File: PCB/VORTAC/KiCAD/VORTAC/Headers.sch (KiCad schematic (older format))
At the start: 27 parts, among them J1 DEBUG, J10 FAN_01_V, J11 FAN_02_V, J12 LED_V, J13 THERM_R, J14 918-418K2023S40001, J15 STEPPER, J16 IO, J2 Molex Micro Fit 3.0, J3 MillMax_004, J4 MillMax_004, J5 USB_HOST, J6 HOTEND, J7 FAN_01, J8 FAN_02, J9 LED

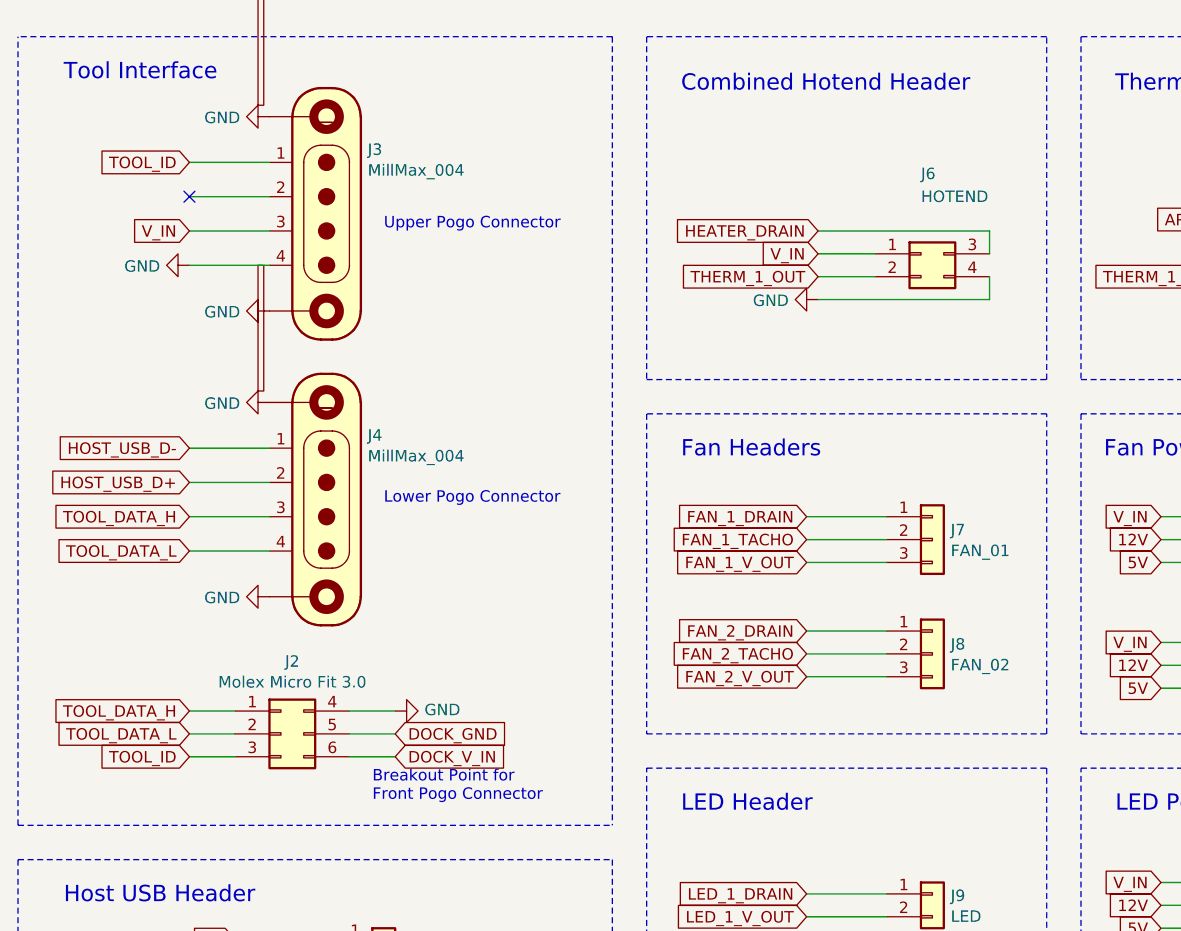
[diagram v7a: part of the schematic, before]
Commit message: Layouting & Footprints
-Improved Thermal Footprint Conductivity
-Improved Component Spacing
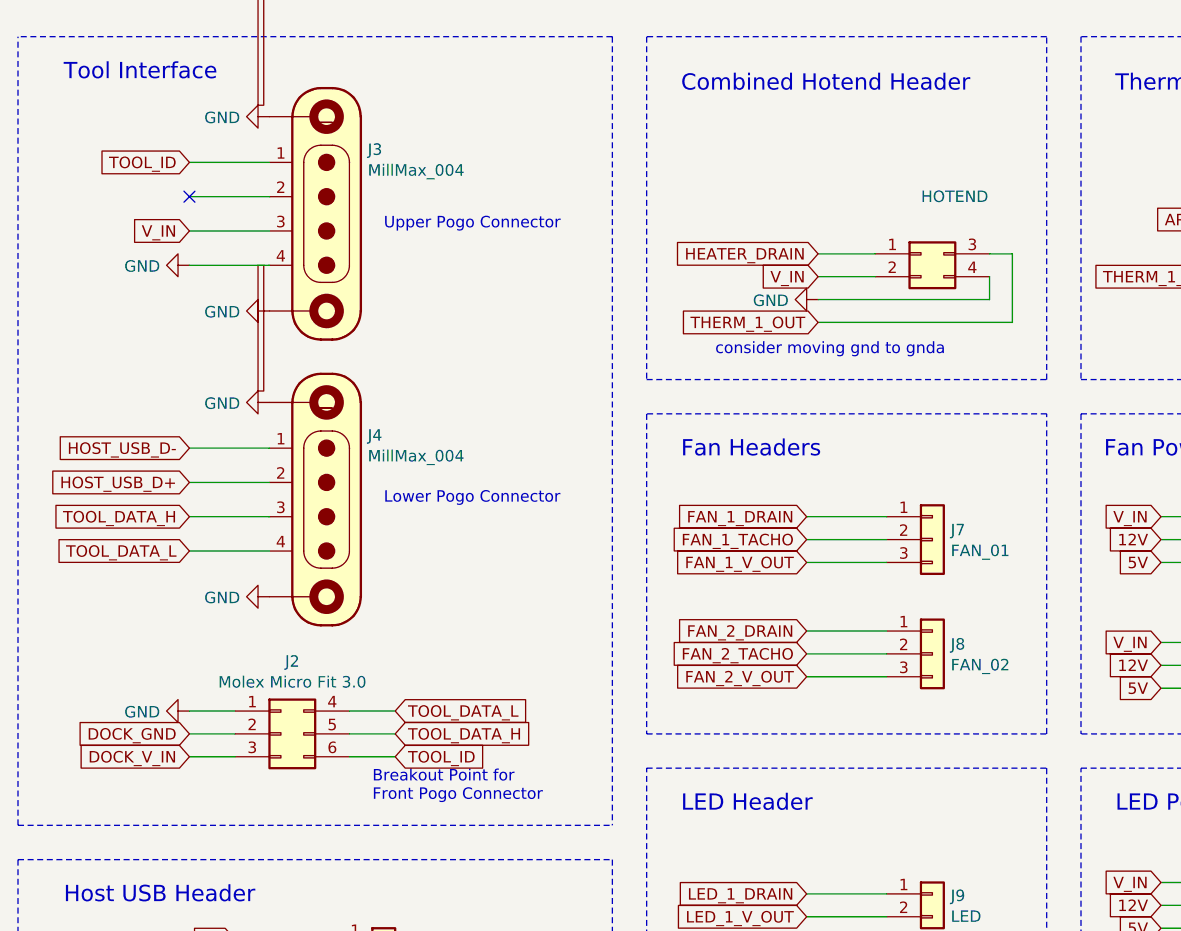
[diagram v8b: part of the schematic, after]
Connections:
- wire segments 91 -> 92
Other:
- note added: "consider moving gnd to gnda"
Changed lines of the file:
@@
 	0    1    1    0
 $EndComp
-Text GLabel 2300 3800 2    50   Input ~ 0
+Text GLabel 1400 3800 0    50   Input ~ 0
 DOCK_V_IN
 $Comp
@@
 Text GLabel 1400 2750 0    50   Input ~ 0
 TOOL_DATA_H
-Text GLabel 1400 3700 0    50   Input ~ 0
+Text GLabel 2300 3600 2    50   Input ~ 0
 TOOL_DATA_L
-Text GLabel 1400 3600 0    50   Input ~ 0
+Text GLabel 2300 3700 2    50   Input ~ 0
 TOOL_DATA_H
-Text GLabel 1400 3800 0    50   Input ~ 0
+Text GLabel 2300 3800 2    50   Input ~ 0
 TOOL_ID
 $Comp
@@
 Text GLabel 1600 4900 0    50   Input ~ 0
 HOST_USB_DRAIN
-Text GLabel 2300 3700 2    50   Input ~ 0
+Text GLabel 1400 3700 0    50   Input ~ 0
 DOCK_GND
 $Comp
@@
 AREF
 Wire Wire Line
-	4900 1500 4900 1600
-Wire Wire Line
-	4150 1500 4900 1500
-Wire Wire Line
 	4900 1800 4900 1700
 Wire Wire Line
@@
 Wire Wire Line
 	4150 1600 4400 1600
+Text GLabel 4150 1700 0    50   Input ~ 0
+V_IN
 Text GLabel 4150 1600 0    50   Input ~ 0
-V_IN
-Text GLabel 4150 1500 0    50   Input ~ 0
 HEATER_DRAIN
-Text GLabel 4150 1700 0    50   Input ~ 0
+Text GLabel 4150 1900 0    50   Input ~ 0
 THERM_1_OUT
 $Comp
@@
 U 1 1 6152EEF9
 P 4600 1600
-F 0 "J6" H 4600 1950 50  0000 L CNN
+F 0 "J6" H 4600 1950 50  0001 L CNN
 F 1 "HOTEND" H 4600 1850 50  0000 L CNN
 F 2 "ToolChanger:Molex_Micro-Fit_3.0_43045-0412_2x02_P3.00mm_Vertical" H 4600 1600 50  0001 C CNN
@@
 L power:GND #PWR0120
 U 1 1 61BCE37C
-P 2300 3600
-F 0 "#PWR0120" H 2300 3350 50  0001 C CNN
-F 1 "GND" V 2305 3472 50  0000 R CNN
-F 2 "" H 2300 3600 50  0001 C CNN
-F 3 "" H 2300 3600 50  0001 C CNN
-	1    2300 3600
-	0    -1   -1   0
+P 1400 3600
+F 0 "#PWR0120" H 1400 3350 50  0001 C CNN
+F 1 "GND" V 1405 3472 50  0000 R CNN
+F 2 "" H 1400 3600 50  0001 C CNN
+F 3 "" H 1400 3600 50  0001 C CNN
+	1    1400 3600
+	0    1    1    0
 $EndComp
 Wire Wire Line
@@
 Wire Wire Line
 	1850 6750 2500 6750
+Text Notes 3700 2050 0    50   ~ 0
+consider moving gnd to gnda
+Wire Wire Line
+	4900 1600 5000 1600
+Wire Wire Line
+	5000 1600 5000 1900
+Wire Wire Line
+	5000 1900 4150 1900
 $EndSCHEMATC
